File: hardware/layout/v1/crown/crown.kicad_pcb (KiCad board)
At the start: 4 copper layers, 60 x 60 mm, 97 parts, among them J1 Main board, J10 DOME_SOCKET, J11 AUX 12V_HEAT, J2 XD_N, J3 XD_E, J4 XD_S, J5 XD_W, J6 PIEZO_NE, J7 PIEZO_NW, J8 PIEZO_SW, J9 PIEZO_SE, U1 STM32G431RBT6, U10 XC6206P332MR, U2 UCC27524ADR, U3 UCC27524ADR, U4 UCC27524ADR, U5 UCC27524ADR, U6 MMC5603NJ, U7 74HC4052D, U8 TLV9062IDR, U9 AS3935-BQFT, Y1 8MHz

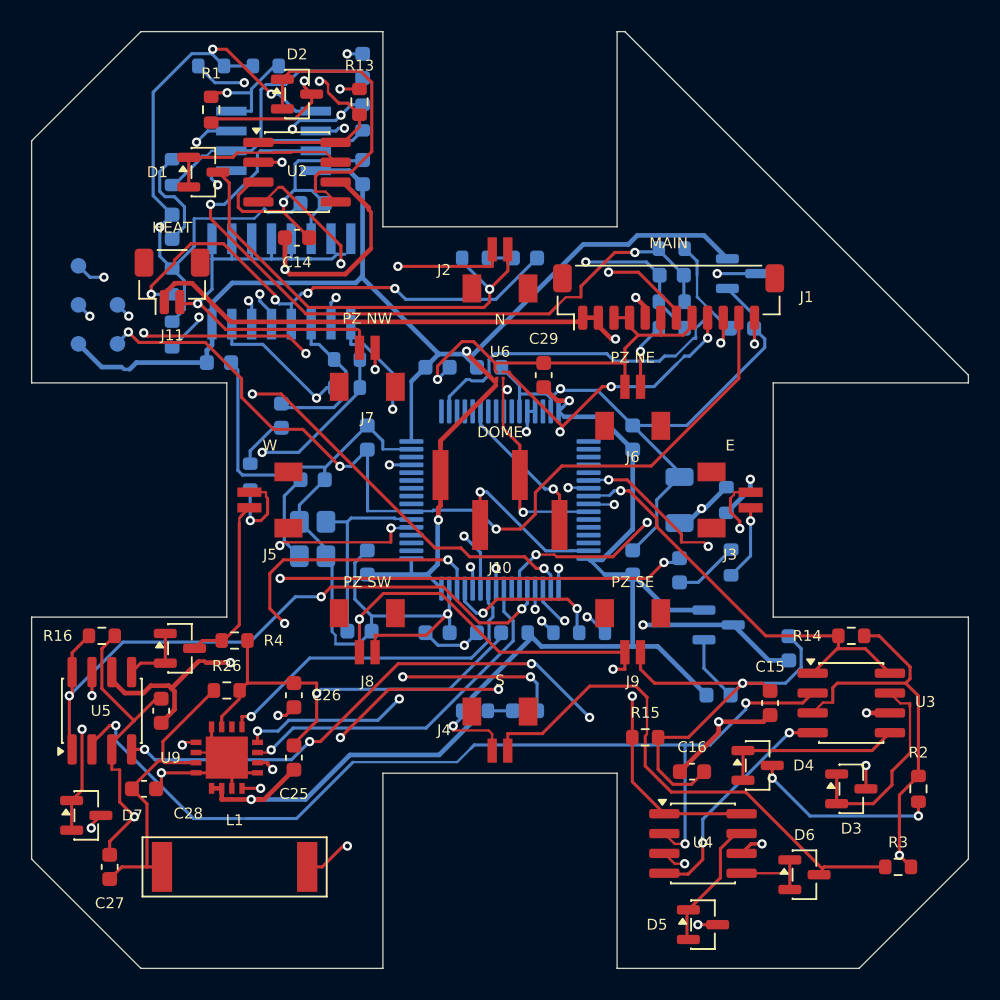
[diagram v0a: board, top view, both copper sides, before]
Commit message: Update RS-485 to poll/response mode with multi-drop addressing, add crown protocol v2 with CRC-protected status, implement wind calibration and rain scaling, fix UCC27524 enable pull-down, add transducer adapter parts
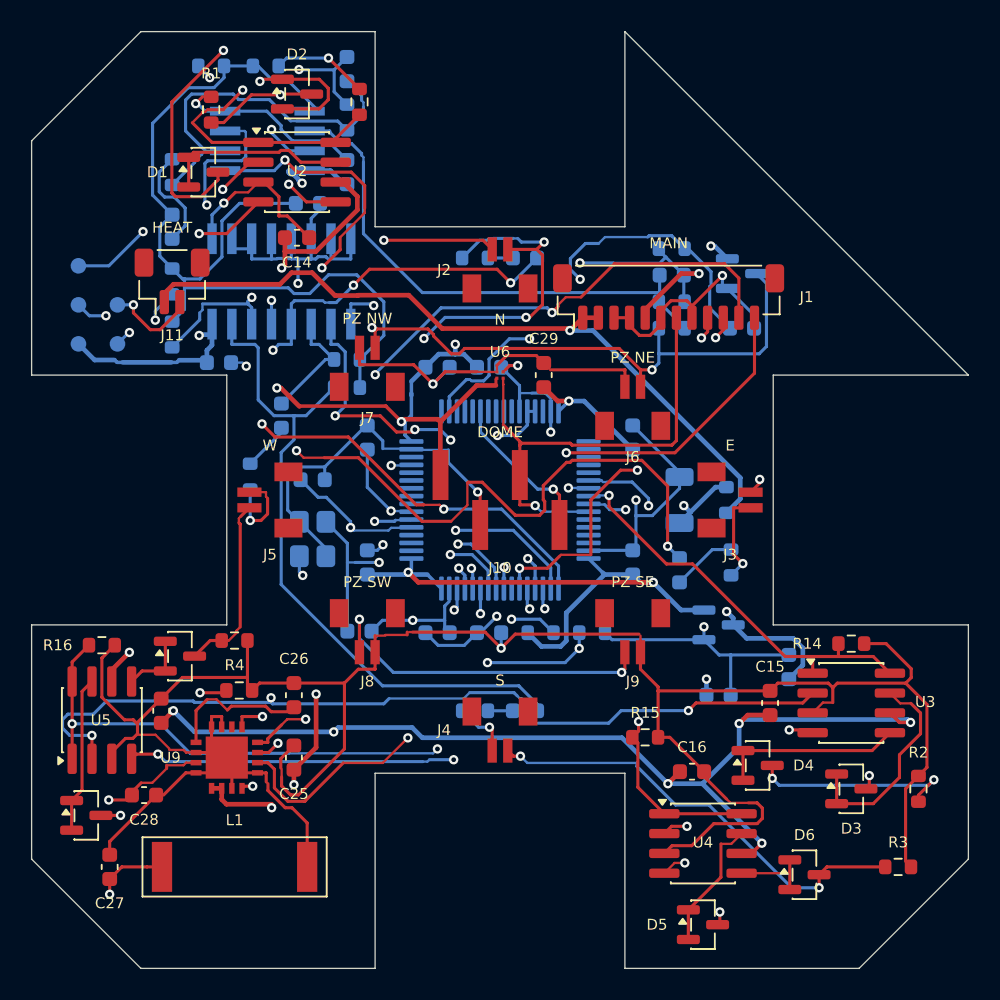
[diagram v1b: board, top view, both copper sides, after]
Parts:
- R13, R14, R15, R16: value 10k -> 4k7
- moved C1 1.20 mm to (48.5, -19.3)
- moved C20 1.02 mm to (20.2, -57.6)
- moved C23 1.00 mm to (20.2, -51.0)
- moved R21 1.00 mm to (20.2, -54.5)
- moved R26 0.80 mm to (13.3, -17.8)
- moved R16 0.60 mm to (4.50, -20.7)
- moved U5 0.60 mm to (4.50, -15.9)
- moved D8 0.50 mm to (9.50, -20.0)
- moved R14 0.50 mm to (52.5, -20.8)
- moved C28 0.40 mm to (7.20, -11.1)
- moved U8 0.40 mm to (15.1, -53.0)
- moved C18 0.30 mm to (17.7, -49.0)
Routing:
- net XD_N_A: track 29.4 -> 59.2 mm, vias 1 -> 4
- net CROWN_NRST: track 58.0 -> 82.6 mm, vias 3 -> 4
- net TX_P: track 141.9 -> 123.1 mm
- net TX_N: track 101.9 -> 115.1 mm, vias 8 -> 6
- net US_VREF: track 71.5 -> 59.7 mm, vias 4 -> 0
- net SWCLK: track 39.5 -> 50.1 mm, vias 3 -> 2
- net PIEZO_OUT: track 47.2 -> 37.0 mm
- net AS_INP: track 19.9 -> 28.6 mm, vias 0 -> 3
- net +3V3: track 175.2 -> 182.8 mm, vias 4 -> 13
- net XD_E_B: track 32.7 -> 39.2 mm
- net VDRV: track 133.8 -> 139.5 mm, vias 6 -> 9
- net XD_S_B: track 34.6 -> 29.0 mm, vias 0 -> 2
- net CROWN_IRQ: track 30.7 -> 25.6 mm
- net XD_N_B: track 31.8 -> 26.9 mm
- net AS_IRQ: track 28.5 -> 23.9 mm, vias 3 -> 2
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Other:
- outline, holes or cut-outs redrawn

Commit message: Update documentation for column-packed breakaway panel, probe LDO rail, mast clamp dimensions, transducer adapter redesign, crown SWD/auto-flash workflow, and enclosure print plate organization
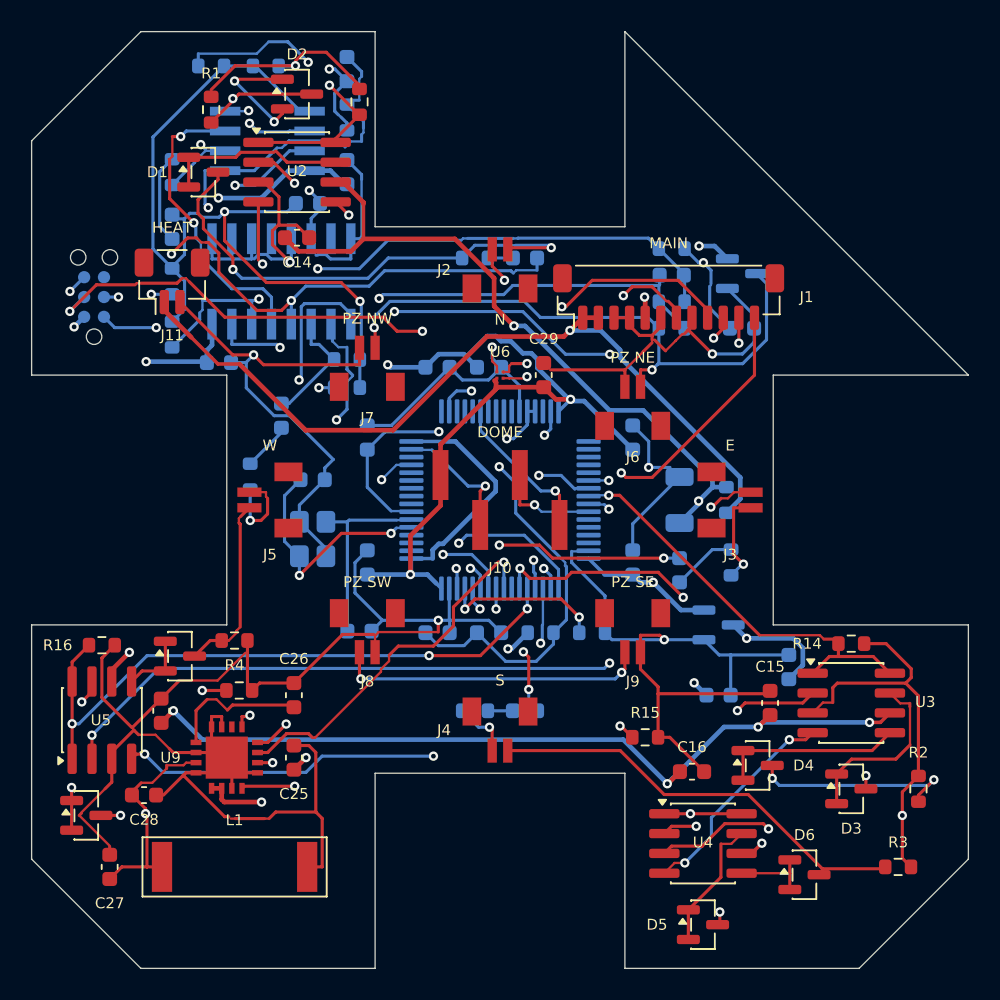
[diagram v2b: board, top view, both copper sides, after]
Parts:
- removed TP1: 3V3, TestPoint:TestPoint_Pad_D1.0mm
- removed TP2: SWDIO, TestPoint:TestPoint_Pad_D1.0mm
- removed TP3: SWCLK, TestPoint:TestPoint_Pad_D1.0mm
- removed TP4: NRST, TestPoint:TestPoint_Pad_D1.0mm
- removed TP5: GND, TestPoint:TestPoint_Pad_D1.0mm
- added J12: SWD, Connector:Tag-Connect_TC2030-IDC-NL_2x03_P1.27mm_Vertical, B.Cu at (4.00, -43.0)
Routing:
- net XD_N_A: track 59.2 -> 32.1 mm, vias 4 -> 2
- net XD_N_B: track 26.9 -> 42.5 mm
- net +3V3: track 182.8 -> 197.9 mm, vias 13 -> 12
- net TX_N: track 115.1 -> 100.9 mm
- net XD_E_RX: track 56.1 -> 45.1 mm
- net MUX_S1: track 23.6 -> 34.2 mm
- net TX_P: track 123.1 -> 112.9 mm, vias 6 -> 8
- net CROWN_BOOT0: track 46.1 -> 36.6 mm, vias 4 -> 3
- net VDRV: track 139.5 -> 130.1 mm, vias 9 -> 8
- net +3V3A: track 61.9 -> 70.5 mm, vias 4 -> 3
- net SWDIO: track 46.7 -> 38.4 mm, vias 3 -> 2
- net CROWN_NRST: track 82.6 -> 74.5 mm
- net I2C_SDA: track 31.3 -> 38.7 mm, vias 1 -> 3
- net PIEZO_INV: track 33.7 -> 41.1 mm, vias 0 -> 2
- net XD_N_OUT_B: track 19.6 -> 27.0 mm, vias 2 -> 3
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
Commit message: Update AGENTS.md, CALIBRATION.md, and README.md for PTFE dome diffuser, probe heater setpoint change to −7.6 °C, crown preamp bias mode, RS-485 fail-safe bias note, and enclosure seal test
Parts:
- added R28: 10k, Resistor_SMD:R_0603_1608Metric, B.Cu at (39.3, -22.4)
- added R29: 10k, Resistor_SMD:R_0603_1608Metric, B.Cu at (38.6, -37.8)
- C25: value 100n 50V -> 1u 50V
- R24: value 1k -> 22k
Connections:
- U1 pad 17: (no net) -> US_VREF
- U1 pad 33: (no net) -> BL_PB12
- U1 pad 44: (no net) -> BL_PA10
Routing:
- net +3V3: track 197.9 -> 176.0 mm, vias 12 -> 8
- net XD_E_RX: track 45.1 -> 64.9 mm, vias 3 -> 4
- net GND: track 307.6 -> 325.9 mm, vias 15 -> 14
- net US_VREF: track 56.0 -> 72.2 mm
- net XD_N_B: track 42.5 -> 28.3 mm
- net US_AMP_FB: track 20.4 -> 32.8 mm
- net VDRV: track 130.1 -> 142.4 mm, vias 8 -> 9
- net CROWN_BOOT0: track 36.6 -> 46.2 mm, vias 3 -> 4
- net TX_N: track 100.9 -> 110.3 mm, vias 6 -> 7
- net XD_N_OUT_B: track 27.0 -> 17.6 mm, vias 3 -> 2
- net XD_S_RX: track 36.6 -> 45.7 mm, vias 4 -> 2
- net +5V: track 37.7 -> 28.8 mm, vias 2 -> 1
- net TX_P: track 112.9 -> 121.0 mm, vias 8 -> 7
- net BL_PA10: track 0.00 -> 7.80 mm, vias 0 -> 2
- net XD_E_B: track 35.3 -> 42.9 mm, vias 3 -> 5
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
